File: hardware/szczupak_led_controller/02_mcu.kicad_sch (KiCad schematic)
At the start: 17 parts, among them IC1 STM32G0B1CBT6, J1 Conn_01x05

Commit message: linked libraries and created pcb stack-up consistent with manufacturer data
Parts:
- removed IC1: STM32G0B1CBT6, FOOTPRINTS:QFP50P900X900X160-48N, symbol Symbols:STM32G0B1CBT6
- removed S1, S2: KMR221G_LFS, FOOTPRINTS:KMR221GLFS, symbol Symbols:KMR221G_LFS
- added IC1: STM32G0B1CBT6, szczupak_led_controller:QFP50P900X900X160-48N, symbol szczupak_led_controller:STM32G0B1CBT6
- added S1, S2: KMR221G_LFS, szczupak_led_controller:KMR221GLFS, symbol szczupak_led_controller:KMR221G_LFS
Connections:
- net +3.3V: now also IC1.4 (VBAT), IC1.5 (VREF+), IC1.6 (VDD/VDDA), S1.1 (NO_1)
- net ADC_12V: now also IC1.14 (PA3)
- net ADC_LED1: now also IC1.11 (PA0)
- net ADC_LED2: now also IC1.12 (PA1)
- net ADC_LED3: now also IC1.13 (PA2)
- net ADC_USB: now also IC1.15 (PA4)
- net CAN_RX: now also IC1.47 (PB8)
- net CAN_TX: now also IC1.48 (PB9)
- net GND: now also IC1.7 (VSS/VSSA), S1.5 (GROUND), S2.2 (COM_1), S2.3 (COM_2), S2.5 (GROUND)
- net I2C1_SCL: now also IC1.29 (PA9)
- net I2C1_SDA: now also IC1.32 (PA10)
- net LED_FAULT: now also IC1.21 (PB2)
- net LED_STATUS: now also IC1.20 (PB1)
- net NRST: now also IC1.10 (PF2-NRST), S2.1 (NO_1)
- net PWM_LED1: now also IC1.17 (PA6)
- net PWM_LED2: now also IC1.18 (PA7)
- net PWM_LED3: now also IC1.19 (PB0)
- net SWCLK_BOOT0: now also IC1.36 (PA14-BOOT0), S1.2 (COM_1)
- net SWDIO: now also IC1.37 (PA15)
- net USART1_RX: now also IC1.46 (PB7)
- net USART1_TX: now also IC1.45 (PB6)
- net USB_DM: now also IC1.33 (PA11_[PA9])
- net USB_DP: now also IC1.34 (PA12_[PA10])

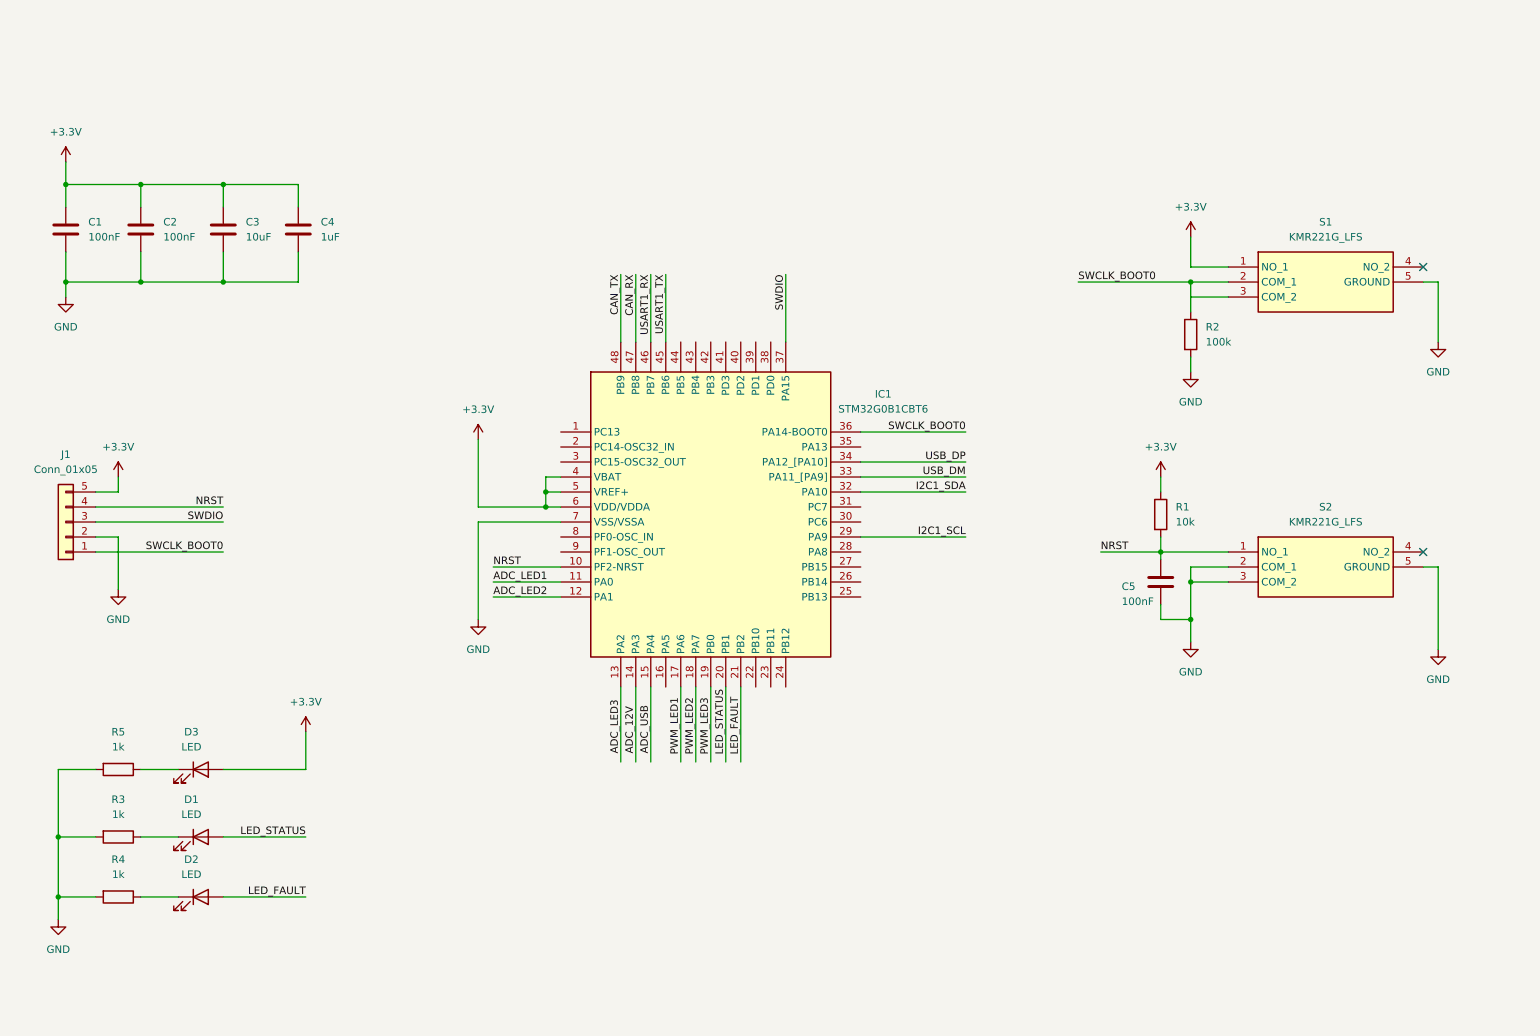
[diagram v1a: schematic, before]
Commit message: #2 Improved schematic readability
Added boxes with proper labels and changed some components placement
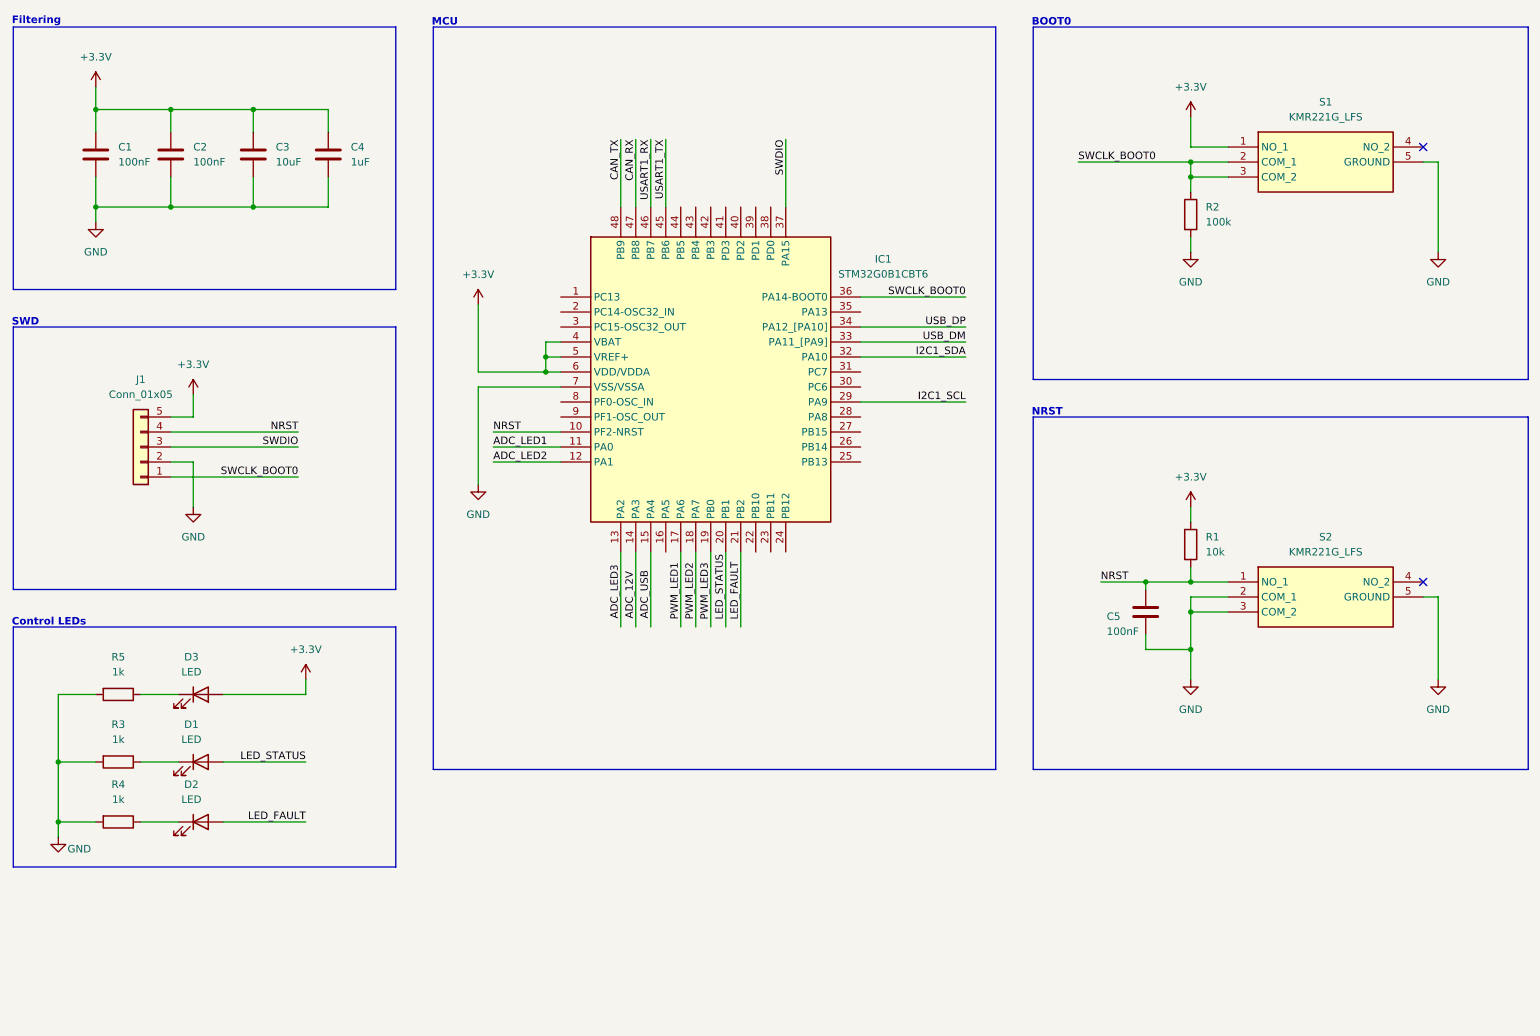
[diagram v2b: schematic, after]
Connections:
- net SWCLK_BOOT0: now also S1.3 (COM_2)
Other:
- note added: "BOOT0"
- note added: "Control LEDs"
- note added: "Filtering"
- note added: "MCU"
- note added: "NRST"
- note added: "SWD"
- moved on the sheet: C1, C2, C3, C4, C5, D1, D2, D3, IC1, J1, R1, R2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

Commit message: #5 #3 Added first version of power_input schematic with some required libraries
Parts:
- removed D3: LED, LED_SMD:LED_0805_2012Metric, symbol Device:LED
- removed R5: 1k, Resistor_SMD:R_0603_1608Metric, symbol Device:R
- added D11: STPS140Z, szczupak_led_controller:SOD3816X145N, symbol Device:D_Schottky
- added JP1: Jumper_2_Open, Jumper:SolderJumper-2_P1.3mm_Open_TrianglePad1.0x1.5mm, symbol Jumper:Jumper_2_Open
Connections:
- net +3.3V: now also D11.1 (K); no longer J1.5 (Pin_5)
- new net: D11.2 (A), JP1.2 (B)
- new net: J1.5 (Pin_5), JP1.1 (A)
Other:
- title: led_driver - 02_mcu -> led_controller - 02_mcu
- moved on the sheet: D1, D2, J1, R3, R4

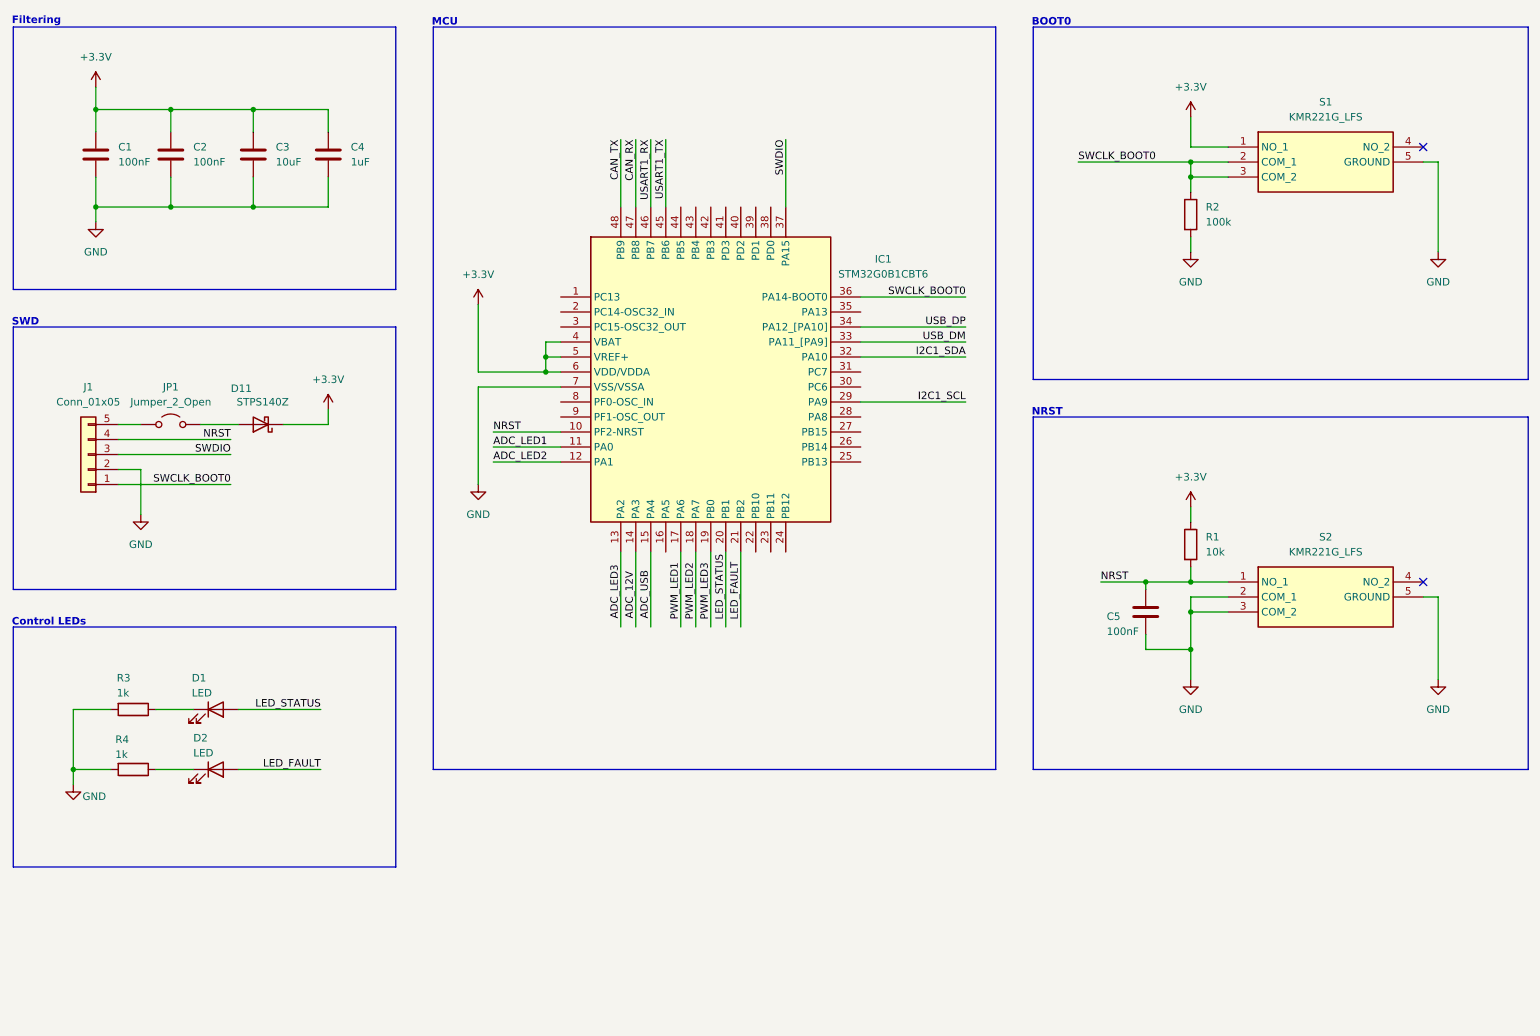
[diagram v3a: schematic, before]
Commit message: #4 #6 Added power output and interfaces schematics
Designed initial placement for most important components on pcb
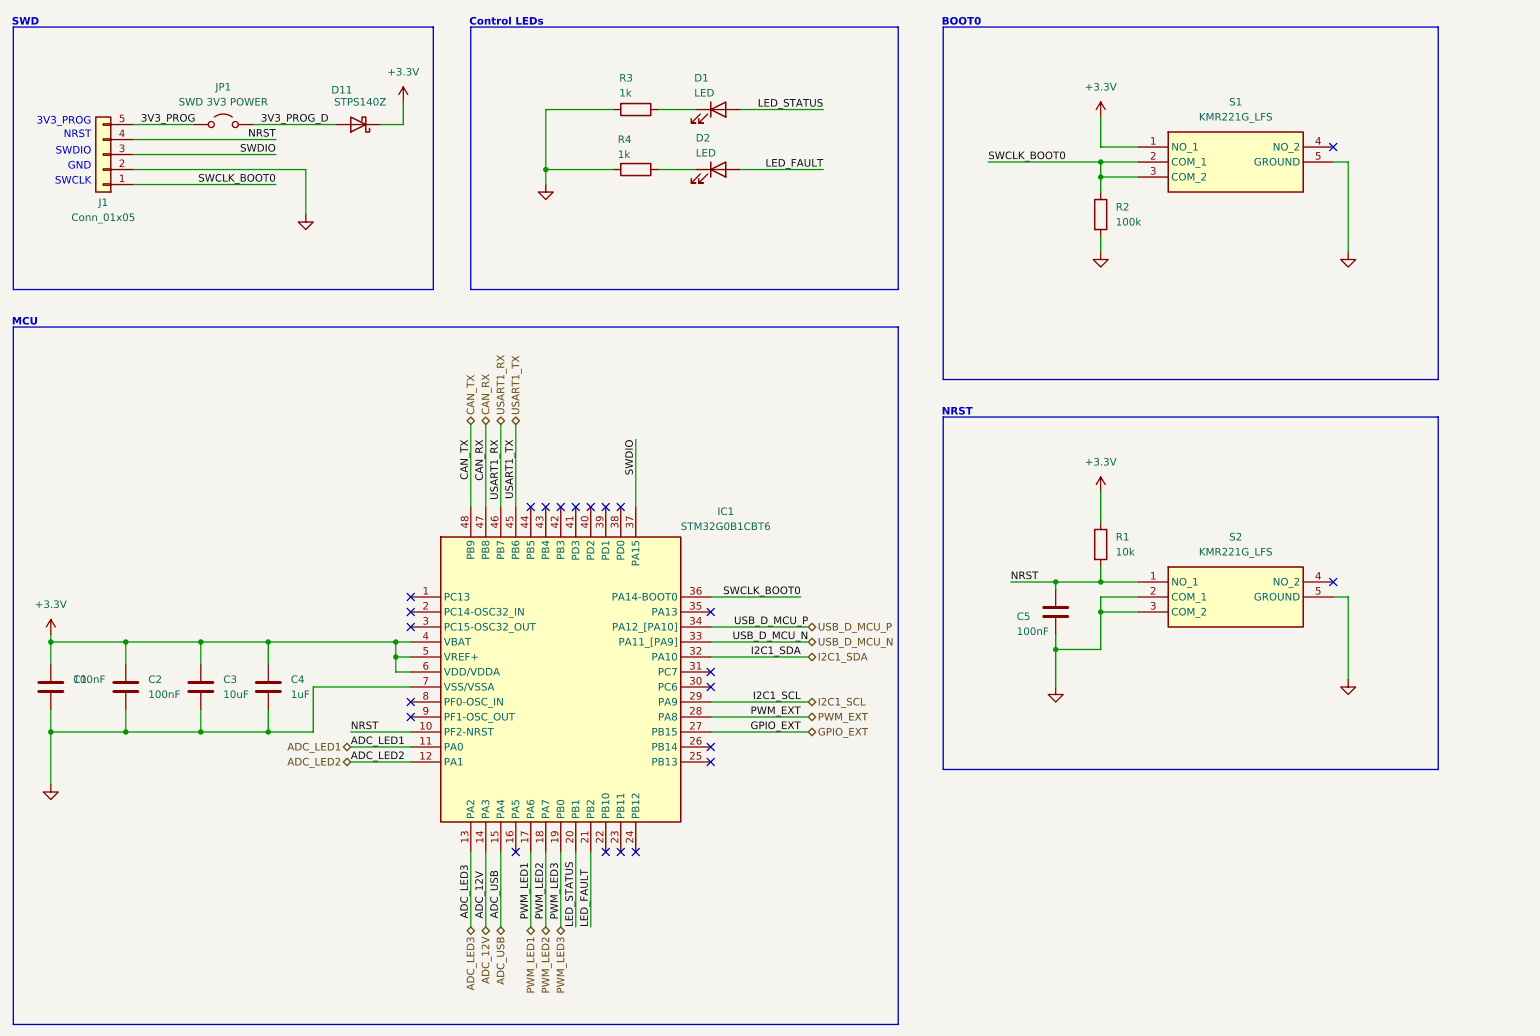
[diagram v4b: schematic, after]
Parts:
- JP1: value Jumper_2_Open -> SWD 3V3 POWER
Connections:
- net 3V3_PROG_D: now reaches D11.2 (A), JP1.2 (B)
- net 3V3_PROG: now reaches J1.5 (Pin_5), JP1.1 (A)
- net GPIO_EXT: now reaches IC1.27 (PB15)
- net PWM_EXT: now reaches IC1.28 (PA8)
- net USB_DM renamed USB_D_MCU_N
- net USB_DP renamed USB_D_MCU_P
- no-connect marks 2 -> 23
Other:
- note added: "3V3_PROG"
- note added: "GND"
- note added: "SWCLK"
- note added: "SWDIO"
- note removed: "Filtering"
- company: (none) -> AGH Marines
- title: led_controller - 02_mcu -> szczupak_led_controller - 02_mcu
- moved on the sheet: C1, C2, C3, C4, C5, D1, D11, D2, IC1, J1, JP1, R1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

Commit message: #8 Finished initial component placement on pcb
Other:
- moved on the sheet: C1, C2, C3, C4

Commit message: #8 Added routing for usb and mcu. Started pouring of power elements
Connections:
- net GND: no longer S1.5 (GROUND), S2.5 (GROUND)
- net LED_FAULT_R: now reaches D2.1 (K), R4.1
- net LED_STATUS_R: now reaches D1.1 (K), R3.1
- no-connect marks 23 -> 25
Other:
- moved on the sheet: D1, D2, R3, R4
